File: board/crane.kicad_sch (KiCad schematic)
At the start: 4 parts

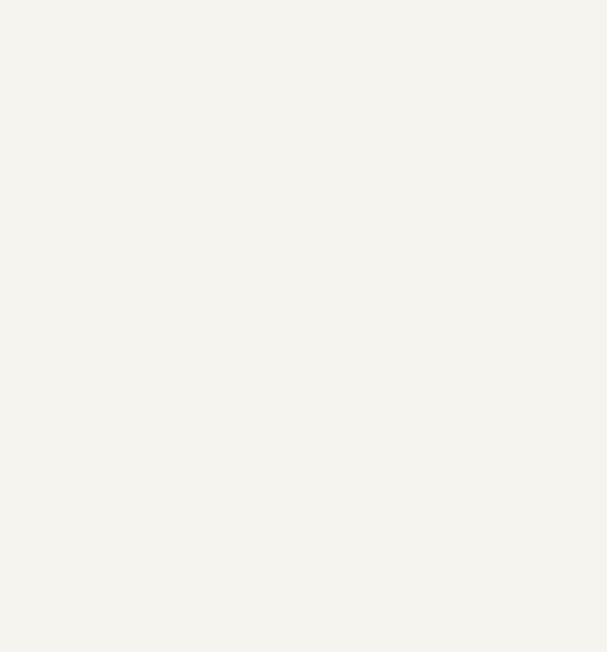
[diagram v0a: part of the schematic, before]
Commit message: updated to Crane V2 Rev A
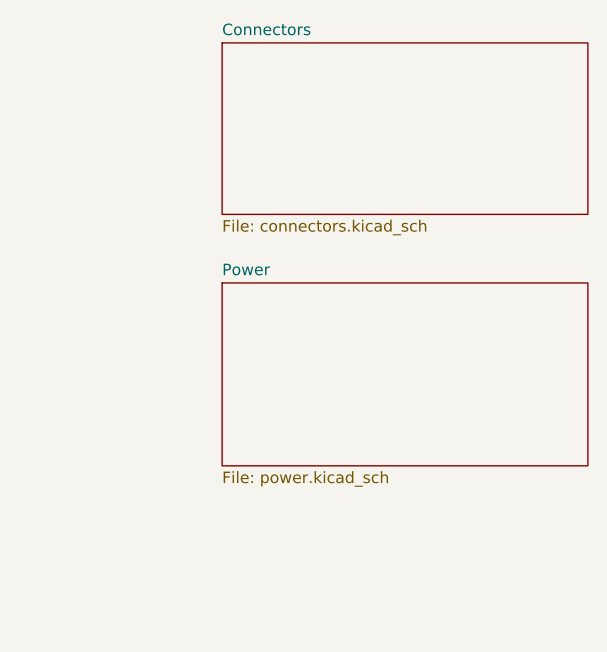
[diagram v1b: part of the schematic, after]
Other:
- added sheet Connectors (connectors.kicad_sch)
- added sheet Power (power.kicad_sch)

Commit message: removed software folder
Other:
- title: (none) -> Crane V2.0 Rev A
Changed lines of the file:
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@@
   (paper "A4")
   (title_block
+    (title "Crane V2.0 Rev A")
     (date "mar. 31 mars 2015")
   )
